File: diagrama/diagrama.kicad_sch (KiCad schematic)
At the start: 9 parts, among them J1 Conn_01x02, U1 LM337_TO3

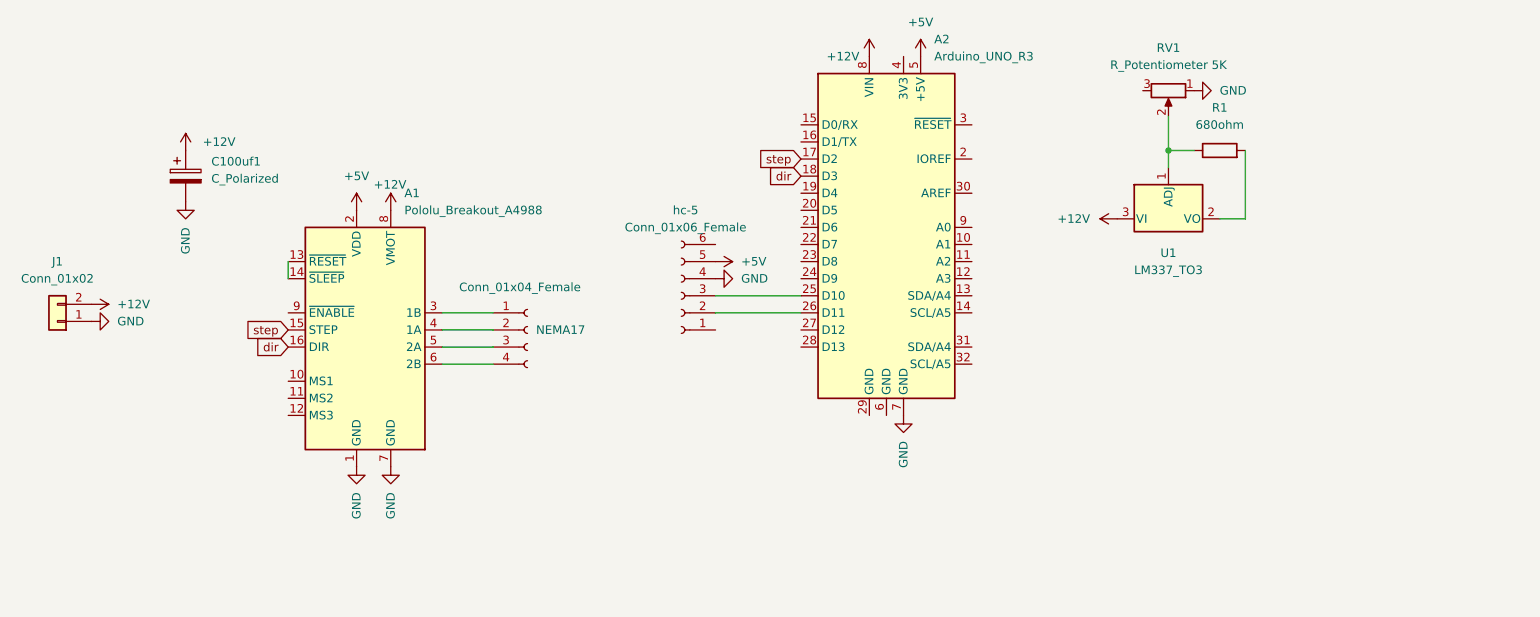
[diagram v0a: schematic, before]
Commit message: eliminado input del ancho y muestra del progreso y cm en el lcd
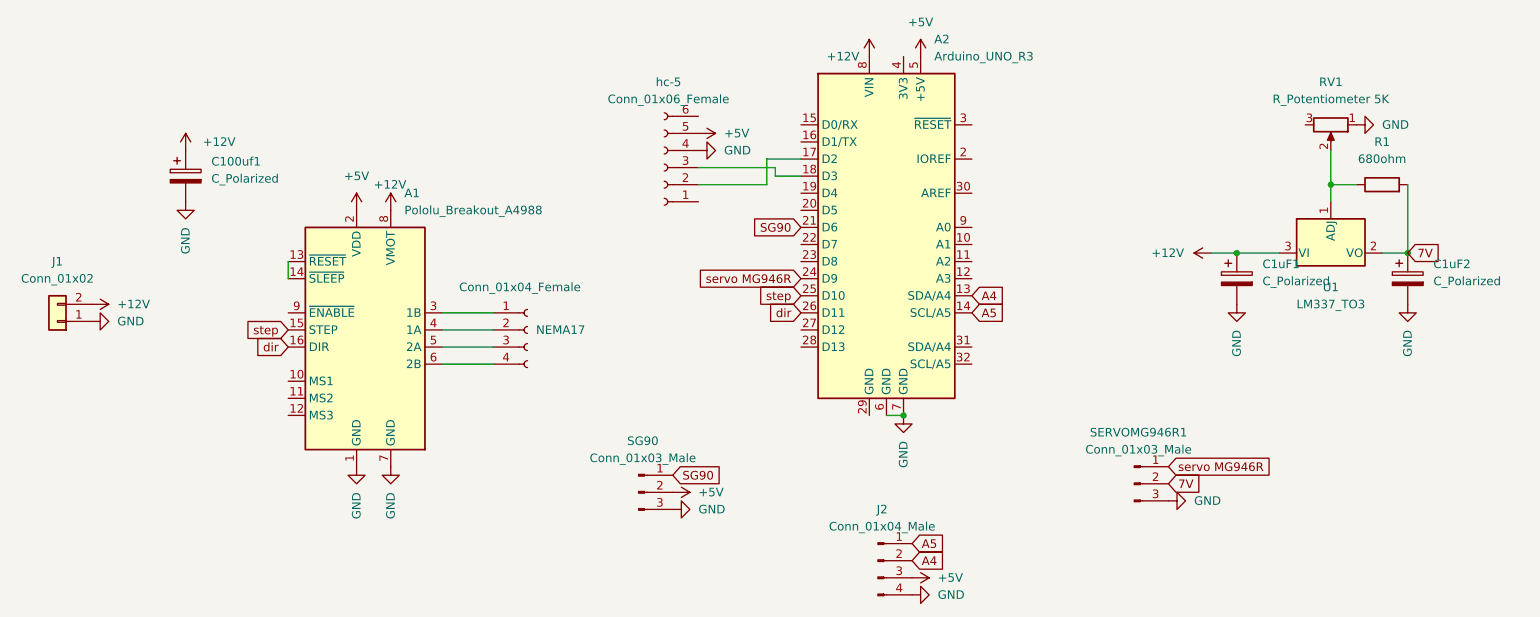
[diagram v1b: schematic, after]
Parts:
- added C1uF1, C1uF2: C_Polarized, Capacitor_THT:C_Radial_D6.3mm_H11.0mm_P2.50mm, symbol Device:C_Polarized
- added J2: Conn_01x04_Male, Connector_PinHeader_2.54mm:PinHeader_1x04_P2.54mm_Vertical, symbol Connector:Conn_01x04_Male
- added SERVOMG946R1, SG90: Conn_01x03_Male, Connector_PinHeader_2.54mm:PinHeader_1x03_P2.54mm_Vertical, symbol Connector:Conn_01x03_Male
- A2: footprint Module:Arduino_UNO_R3 -> Module:Arduino_UNO_R3 modificado
- C100uf1: footprint Capacitor_SMD:CP_Elec_6.3x9.9 -> Capacitor_THT:C_Radial_D6.3mm_H11.0mm_P2.50mm
- U1: footprint Package_TO_SOT_THT:TO-3 -> Package_TO_SOT_THT:TO-3-nuevo
- hc-5: footprint Connector_PinSocket_1.00mm:PinSocket_1x06_P1.00mm_Vertical -> Connector_PinSocket_2.54mm:PinSocket_1x06_P2.54mm_Vertical
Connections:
- net +12V: now also C1uF1.1
- net +5V: now also J2.3 (Pin_3), SG90.2 (Pin_2)
- net GND: now also A2.6 (GND), C1uF1.2, C1uF2.2, J2.4 (Pin_4), SERVOMG946R1.3 (Pin_3), SG90.3 (Pin_3)
- net dir: now also A2.26 (D11); no longer A2.18 (D3)
- net step: now also A2.25 (D10); no longer A2.17 (D2)
- net at hc-5.2 (Pin_2): now also A2.17 (D2); no longer A2.26 (D11)
- net at hc-5.3 (Pin_3): now also A2.18 (D3); no longer A2.25 (D10)
- net 7V: now reaches R1.2, U1.2 (VO)
- net 7V: now also C1uF2.1, SERVOMG946R1.2 (Pin_2)
- net A4: now reaches A2.13 (SDA/A4)
- net A4: now also J2.2 (Pin_2)
- net A5: now reaches A2.14 (SCL/A5)
- net A5: now also J2.1 (Pin_1)
- net SG90: now reaches A2.21 (D6)
- net SG90: now also SG90.1 (Pin_1)
- net servo MG946R: now reaches A2.24 (D9)
- net servo MG946R: now also SERVOMG946R1.1 (Pin_1)
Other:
- moved on the sheet: R1, RV1, U1, hc-5
